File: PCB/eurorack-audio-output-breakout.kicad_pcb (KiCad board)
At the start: 2 copper layers, 18.4 x 50.5 mm, 12 parts, among them J1 Conn_01x04_Pin, J10 A, J11 B, J12 Conn_01x05_Pin, J3 Conn_01x04_Pin, J4 Conn_01x02_Pin, J5 Conn_01x05_Pin, U1 TL072

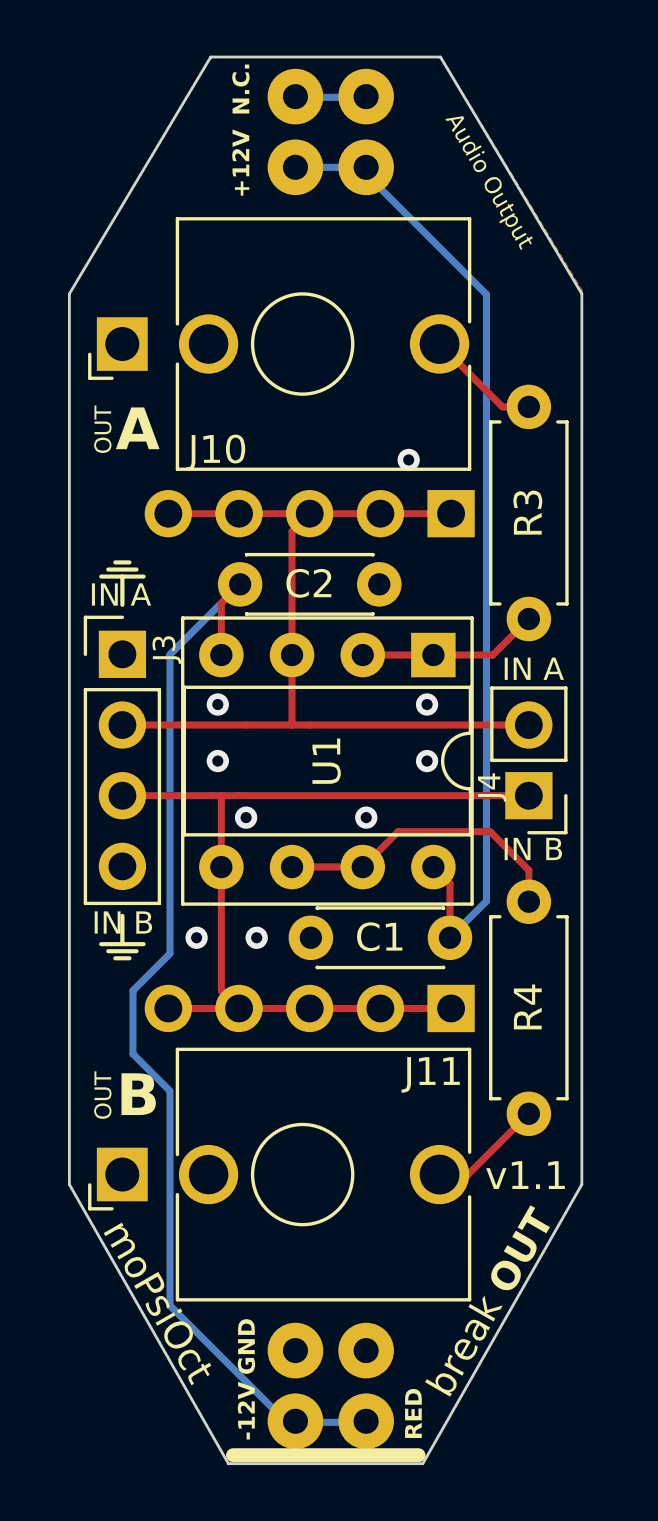
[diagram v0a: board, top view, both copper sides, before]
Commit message: Fix placement with reference
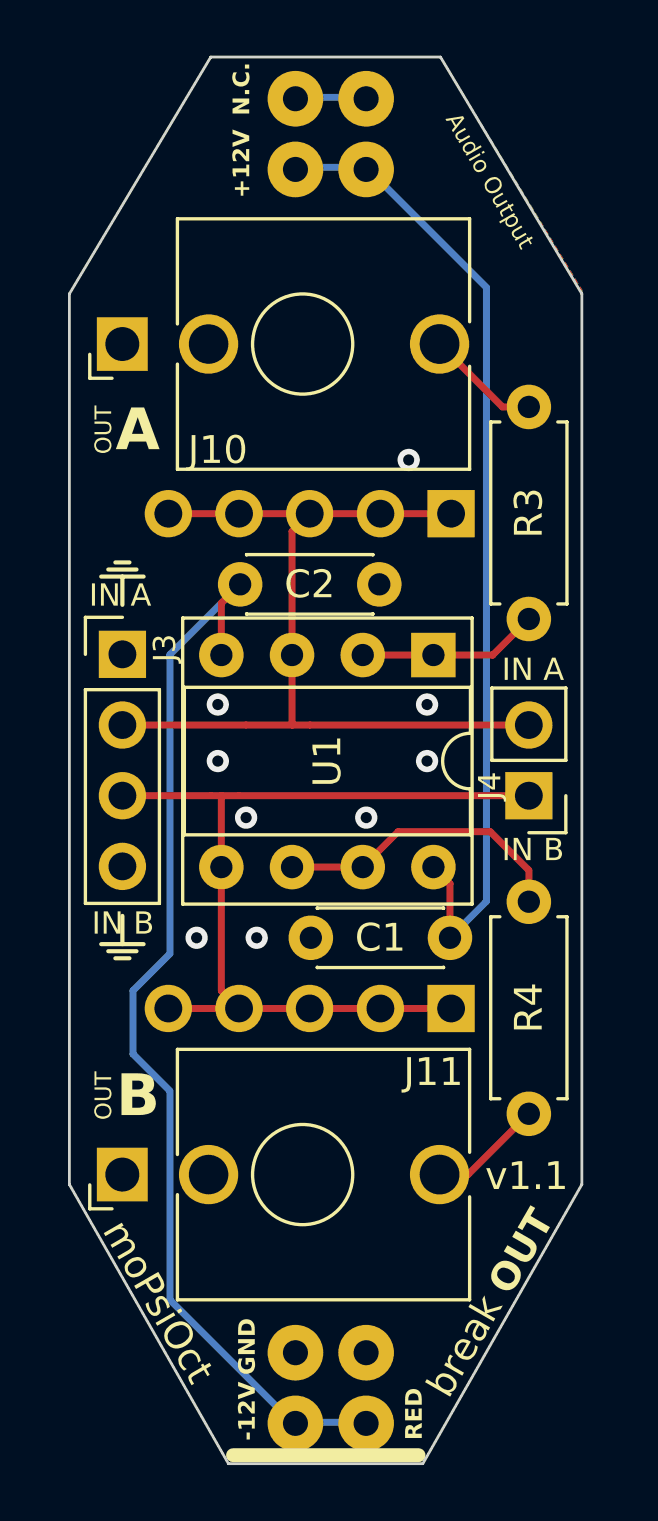
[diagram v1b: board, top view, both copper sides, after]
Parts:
- moved J1 0.08 mm to (191.8, 88.9)
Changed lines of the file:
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@@
 	(footprint "moPsy:Breadboard Power Connector"
 		(layer "B.Cu")
-		(at 191.77 88.824 180)
+		(at 191.77 88.9 180)
 		(property "Reference" "J1"
 			(at 0.757 19.101 0)
@@
 	)
 	(segment
-		(start 196.85 93.94)
-		(end 195.54 95.25)
+		(start 192.532 67.564)
+		(end 196.85 71.882)
 		(width 0.25)
 		(layer "B.Cu")
@@
 	)
 	(segment
-		(start 192.283 67.564)
-		(end 196.85 72.131)
+		(start 196.85 93.94)
+		(end 195.54 95.25)
 		(width 0.25)
 		(layer "B.Cu")
@@
 	)
 	(segment
-		(start 196.85 72.131)
+		(start 196.85 71.882)
 		(end 196.85 93.94)
 		(width 0.25)
@@
 	(segment
 		(start 189.743 67.564)
-		(end 192.283 67.564)
+		(end 192.532 67.564)
 		(width 0.25)
 		(layer "B.Cu")
@@
 	)
 	(segment
-		(start 184.15 97.149649)
-		(end 185.476 95.823649)
+		(start 185.476 108.26)
+		(end 185.476 100.7546)
 		(width 0.25)
 		(layer "B.Cu")
@@
 	)
 	(segment
-		(start 184.15 99.4286)
-		(end 184.15 97.149649)
+		(start 185.476 85.074)
+		(end 188 82.55)
 		(width 0.25)
 		(layer "B.Cu")
@@
 	)
 	(segment
-		(start 185.476 95.823649)
-		(end 185.476 85.074)
+		(start 192.537 112.6596)
+		(end 189.8756 112.6596)
 		(width 0.25)
 		(layer "B.Cu")
@@
 	)
 	(segment
-		(start 192.537 112.6596)
-		(end 189.6691 112.6596)
+		(start 184.15 97.149649)
+		(end 185.476 95.823649)
 		(width 0.25)
 		(layer "B.Cu")
@@
 	)
 	(segment
-		(start 185.476 100.7546)
-		(end 184.15 99.4286)
+		(start 184.15 99.4286)
+		(end 184.15 97.149649)
 		(width 0.25)
 		(layer "B.Cu")
@@
 	)
 	(segment
-		(start 189.6691 112.6596)
-		(end 185.476 108.4665)
+		(start 185.476 95.823649)
+		(end 185.476 85.074)
 		(width 0.25)
 		(layer "B.Cu")
@@
 	)
 	(segment
-		(start 185.476 108.4665)
-		(end 185.476 100.7546)
+		(start 189.8756 112.6596)
+		(end 185.476 108.26)
 		(width 0.25)
 		(layer "B.Cu")
@@
 	)
 	(segment
-		(start 185.476 85.074)
-		(end 188 82.55)
+		(start 185.476 100.7546)
+		(end 184.15 99.4286)
 		(width 0.25)
 		(layer "B.Cu")
